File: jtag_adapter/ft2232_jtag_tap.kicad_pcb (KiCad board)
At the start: 2 copper layers, 50 x 30 mm, 41 parts, among them J1 USB_C_Receptacle_USB2.0, J2 Conn_ARM_JTAG_SWD_20, U1 93AA56BT-I/OT, U2 FT232HL, Y1 Crystal_GND24

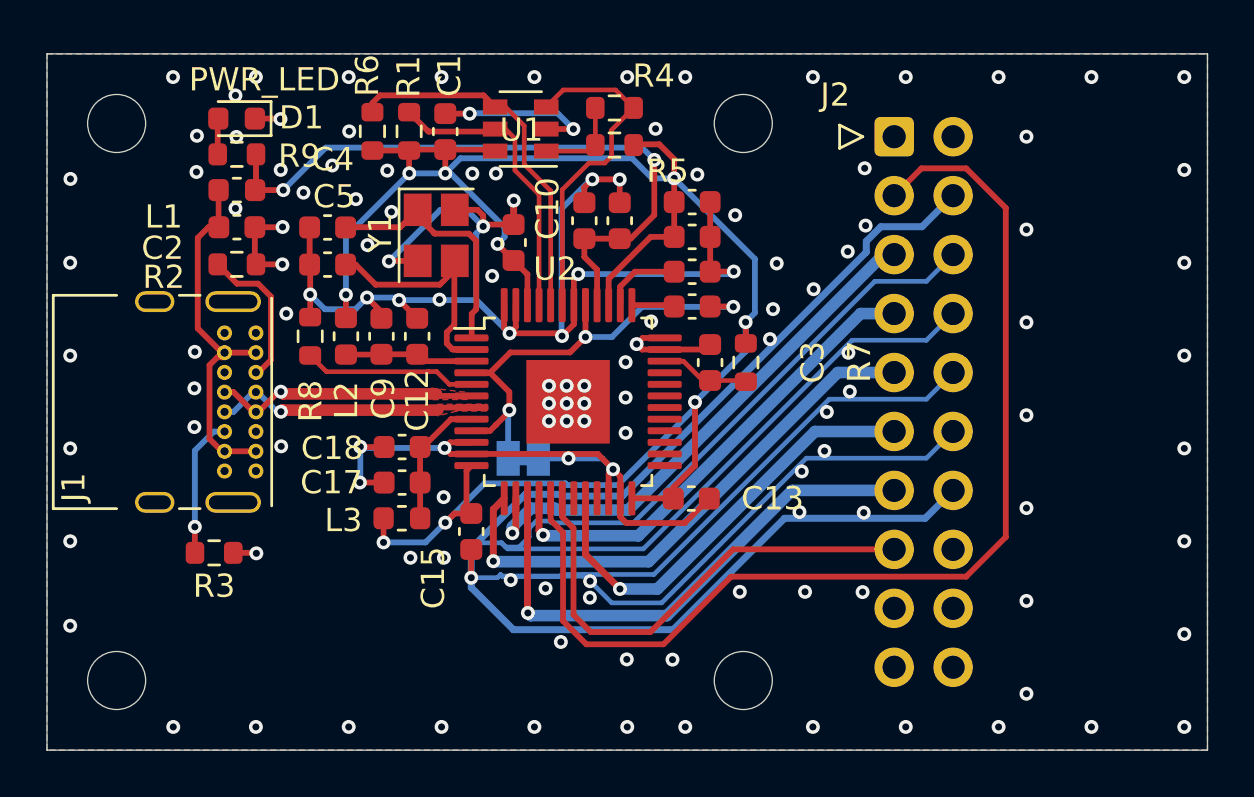
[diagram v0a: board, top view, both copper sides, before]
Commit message: fix SRST/TRST and remove unnecessary files
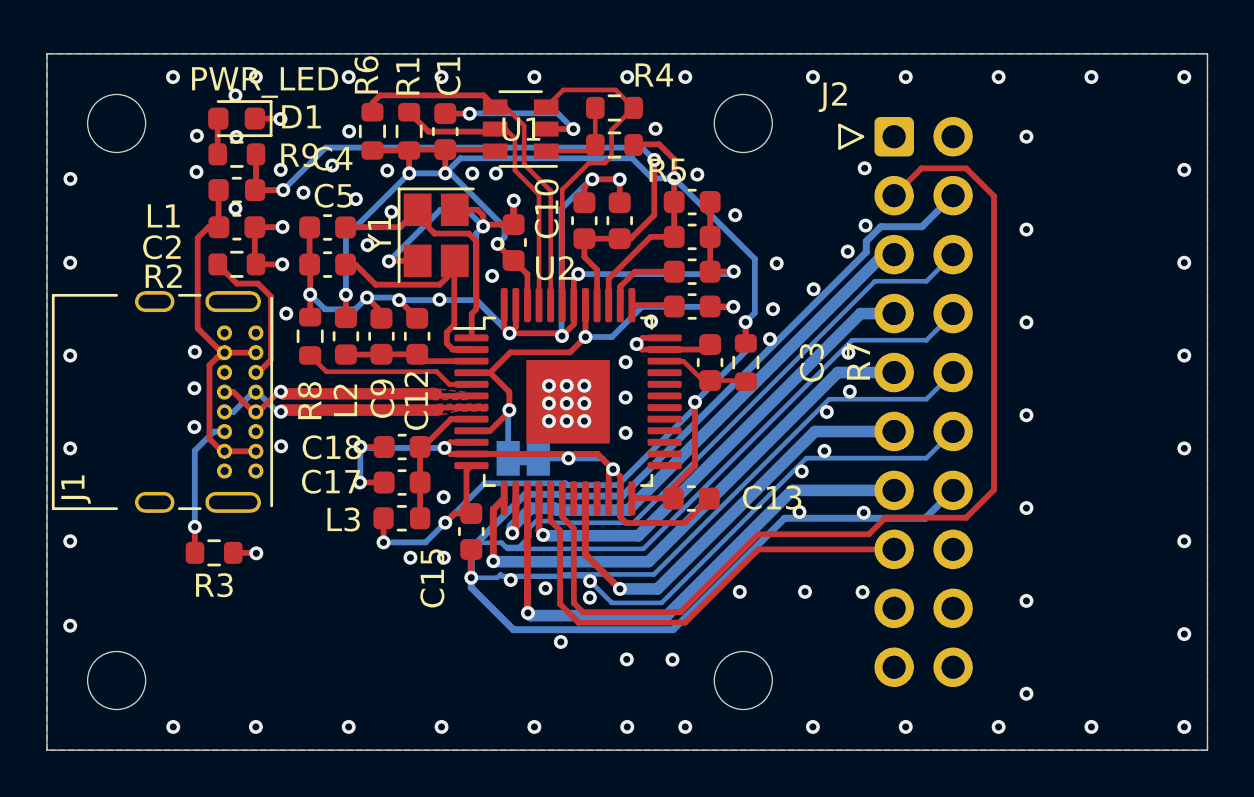
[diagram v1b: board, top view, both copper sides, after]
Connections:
- J2 pad 15: /~TRST -> /~SRST
- J2 pad 3: /~SRST -> /~TRST
- U2 pad 49: GND -> (no net)
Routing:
- net /~SRST: track 47.1 -> 20.8 mm
- net /~TRST: track 20.8 -> 43.1 mm
- net GND: vias 133 -> 124
- net (no net): vias 0 -> 9

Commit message: fix gnd
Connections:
- U2 pad 49: (no net) -> GND
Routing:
- net GND: vias 124 -> 133
- net (no net): vias 9 -> 0
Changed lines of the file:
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@@
     (pad "" smd roundrect (at -1.2 0) (size 0.97 0.97) (layers F.Paste) (roundrect_rratio 0.25))
     (pad "" smd roundrect (at -1.2 -1.2) (size 0.97 0.97) (layers F.Paste) (roundrect_rratio 0.25))
-    (pad 49 smd rect (at 0 0) (size 3.6 3.6) (layers F.Cu F.Mask))
+    (pad 49 smd rect (at 0 0) (size 3.6 3.6) (layers F.Cu F.Mask)
+      (net 1 GND))
     (pad 48 smd roundrect (at -2.75 -4.1625) (size 0.3 1.475) (layers F.Cu F.Paste F.Mask) (roundrect_rratio 0.25)
       (net 1 GND))
@@
   (gr_line (start 50 100) (end 100 100) (layer Edge.Cuts) (width 0.05))
   (gr_line (start 50 100) (end 50 130) (layer Edge.Cuts) (width 0.05))
-  (via (at 72.39 115.062) (size 0.6) (drill 0.3) (layers F.Cu B.Cu) (net 0))
-  (via (at 71.628 115.062) (size 0.6) (drill 0.3) (layers F.Cu B.Cu) (net 0))
-  (via (at 71.628 115.824) (size 0.6) (drill 0.3) (layers F.Cu B.Cu) (net 0))
-  (via (at 72.39 115.824) (size 0.6) (drill 0.3) (layers F.Cu B.Cu) (net 0))
-  (via (at 73.152 115.824) (size 0.6) (drill 0.3) (layers F.Cu B.Cu) (net 0))
-  (via (at 73.152 115.062) (size 0.6) (drill 0.3) (layers F.Cu B.Cu) (net 0))
-  (via (at 73.152 114.3) (size 0.6) (drill 0.3) (layers F.Cu B.Cu) (net 0))
-  (via (at 72.39 114.3) (size 0.6) (drill 0.3) (layers F.Cu B.Cu) (net 0))
-  (via (at 71.628 114.3) (size 0.6) (drill 0.3) (layers F.Cu B.Cu) (net 0))
+  (via (at 72.39 115.062) (size 0.6) (drill 0.3) (layers F.Cu B.Cu) (net 1))
+  (via (at 71.628 115.062) (size 0.6) (drill 0.3) (layers F.Cu B.Cu) (net 1))
+  (via (at 71.628 115.824) (size 0.6) (drill 0.3) (layers F.Cu B.Cu) (net 1))
+  (via (at 72.39 115.824) (size 0.6) (drill 0.3) (layers F.Cu B.Cu) (net 1))
+  (via (at 73.152 115.824) (size 0.6) (drill 0.3) (layers F.Cu B.Cu) (net 1))
+  (via (at 73.152 115.062) (size 0.6) (drill 0.3) (layers F.Cu B.Cu) (net 1))
+  (via (at 73.152 114.3) (size 0.6) (drill 0.3) (layers F.Cu B.Cu) (net 1))
+  (via (at 72.39 114.3) (size 0.6) (drill 0.3) (layers F.Cu B.Cu) (net 1))
+  (via (at 71.628 114.3) (size 0.6) (drill 0.3) (layers F.Cu B.Cu) (net 1))
   (via (at 72.68 103.24) (size 0.6) (drill 0.3) (layers F.Cu B.Cu) (net 1))
   (segment (start 71.51 103.24) (end 72.68 103.24) (width 0.25) (layer F.Cu) (net 1))
@@
     (connect_pads (clearance 0.2))
     (min_thickness 0.127)
-    (fill yes (arc_segments 32) (thermal_gap 0.2) (thermal_bridge_width 0.2))
+    (fill (arc_segments 32) (thermal_gap 0.2) (thermal_bridge_width 0.2))
     (polygon
       (pts
@@
     (connect_pads (clearance 0.2))
     (min_thickness 0.127)
-    (fill yes (arc_segments 32) (thermal_gap 0.2) (thermal_bridge_width 0.2))
+    (fill (arc_segments 32) (thermal_gap 0.2) (thermal_bridge_width 0.2))
     (polygon
       (pts
@@
     (connect_pads yes (clearance 0.2))
     (min_thickness 0.2)
-    (fill yes (arc_segments 32) (thermal_gap 0.2) (thermal_bridge_width 0.3))
+    (fill (arc_segments 32) (thermal_gap 0.2) (thermal_bridge_width 0.3))
     (polygon
       (pts
@@
     (connect_pads yes (clearance 0.2))
     (min_thickness 0.2)
-    (fill yes (arc_segments 32) (thermal_gap 0.2) (thermal_bridge_width 0.3))
+    (fill (arc_segments 32) (thermal_gap 0.2) (thermal_bridge_width 0.3))
     (polygon
       (pts
